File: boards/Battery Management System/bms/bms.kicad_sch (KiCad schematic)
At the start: 25 parts, among them J1 Screw_Terminal_01x05, J2 1986660-2, J3 1986660-2, K1 HE1AN-W-DC6V-Y6, U1 BD48L32G, U2 BD48L32G, U3 BD48L32G, U4 BD48L32G, U5 SN74HC08DR, U6 TL071HIDBVR

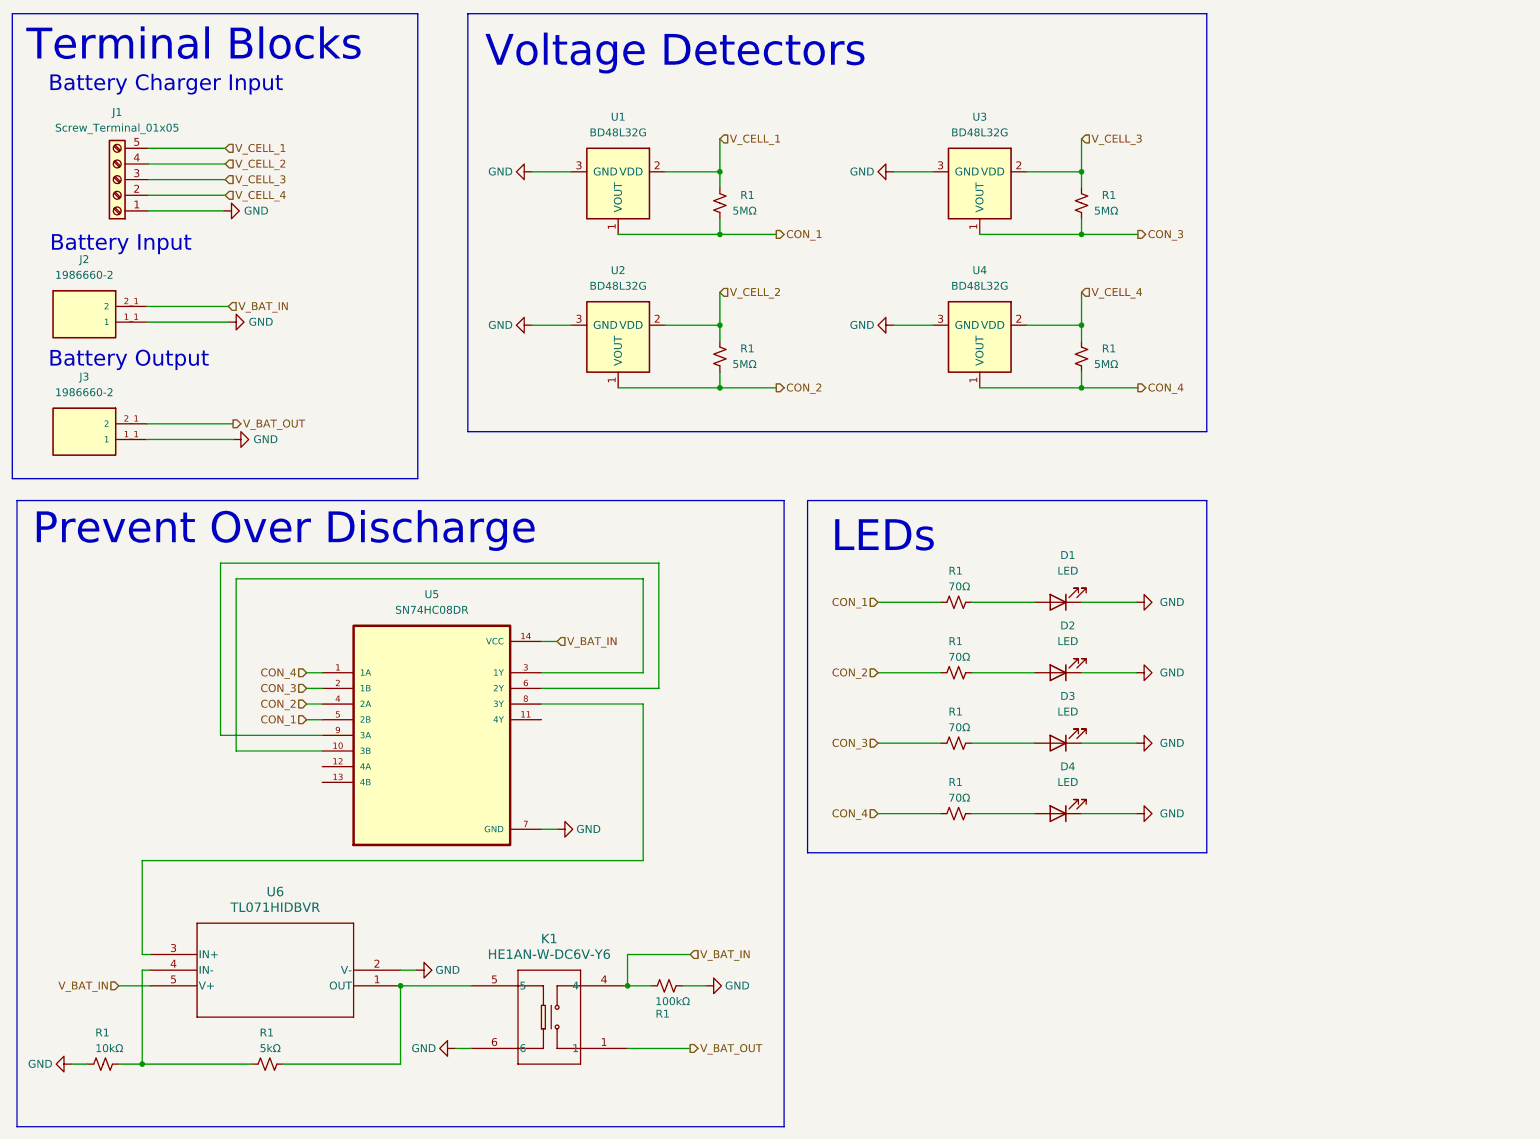
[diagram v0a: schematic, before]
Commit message: Removed Relay
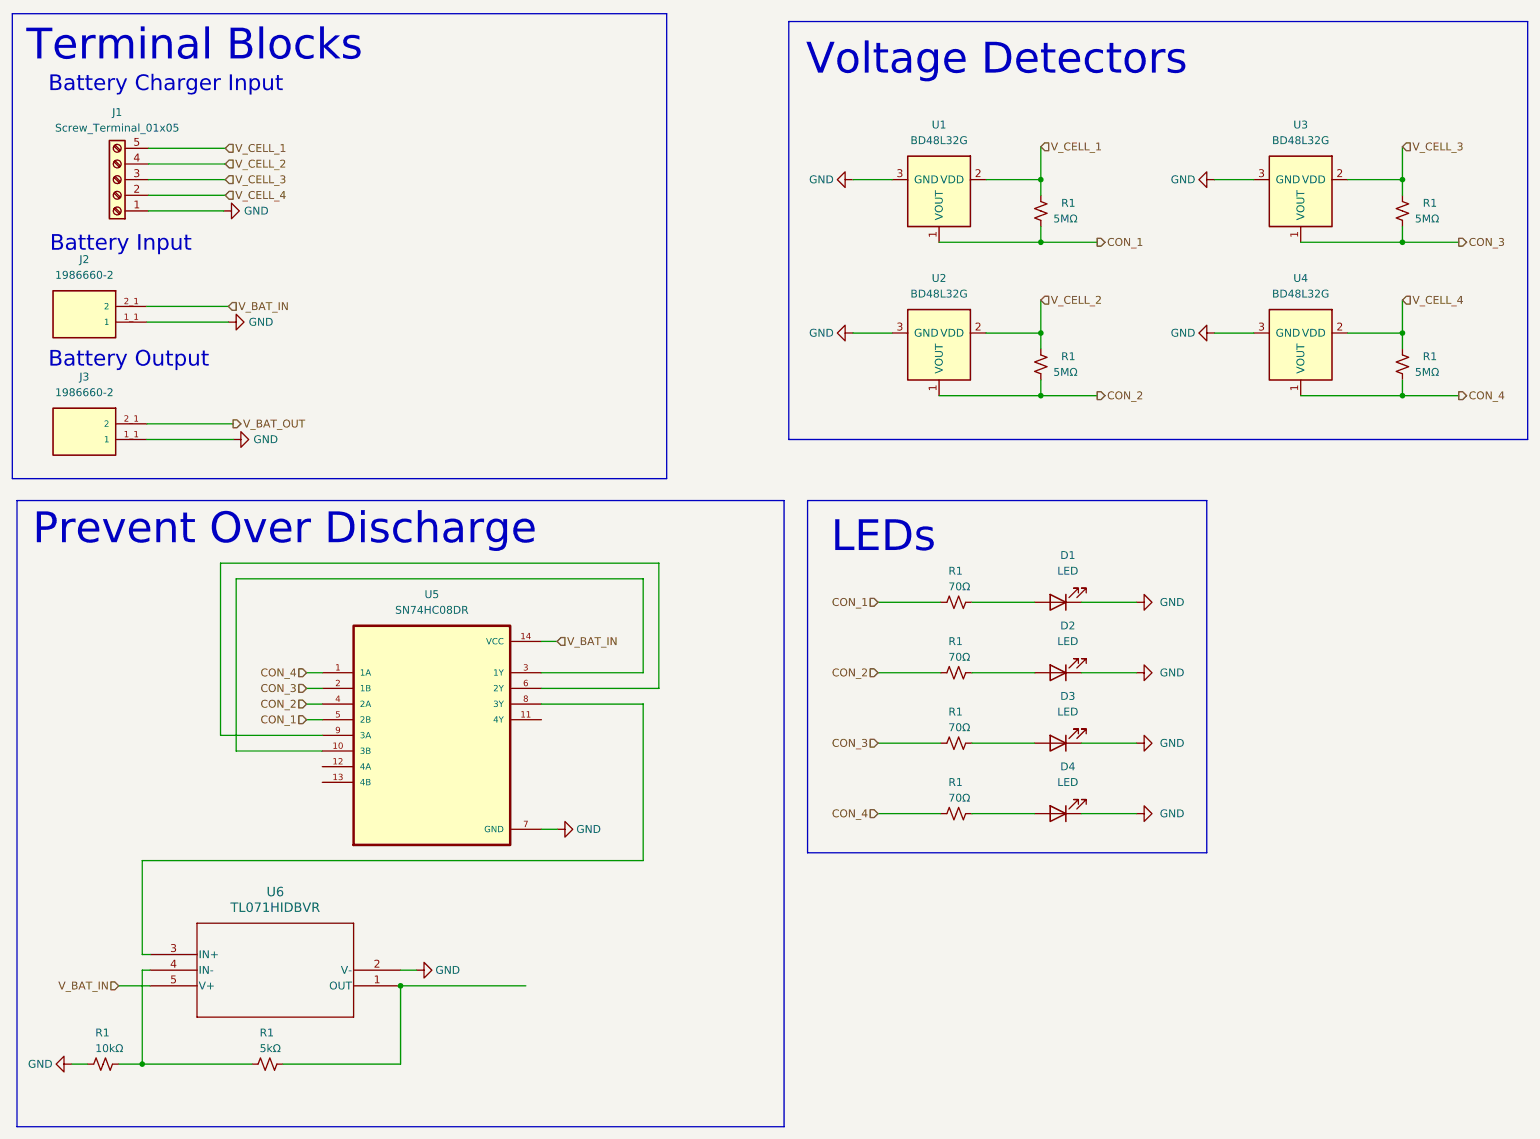
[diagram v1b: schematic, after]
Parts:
- removed K1: HE1AN-W-DC6V-Y6, HE1AN_W_DC6V_Y6:HE1AN-W-DC6V_PAN, symbol 2024-03-08_00-12-08:HE1AN-W-DC6V-Y6
- removed R1: 100kΩ, Resistor_SMD:R_0805_2012Metric, symbol Device:R_Small_US
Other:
- moved on the sheet: R1, U1, U2, U3, U4

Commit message: New Schematic
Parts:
- removed J2, J3: 1986660-2, 1986660_2a:TE_1986660-2, symbol 1986660-2:1986660-2
- removed R1: 10kΩ, Resistor_SMD:R_0805_2012Metric, symbol Device:R_Small_US
- removed R1: 5kΩ, Resistor_SMD:R_0805_2012Metric, symbol Device:R_Small_US
- removed U6: TL071HIDBVR, TL071HIDBVR:SOT23_DBV_5_TEX-L, symbol TL071HIDBVR:TL071HIDBVR
- J1: value Screw_Terminal_01x05 -> Screw_Terminal_01x06; symbol Connector:Screw_Terminal_01x05 -> Connector:Screw_Terminal_01x06
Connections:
- net V_OUT: now reaches U5.8 (3Y)
- net V_OUT: now also J1.6 (Pin_6)
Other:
- note removed: "Battery Input"
- note removed: "Battery Output"

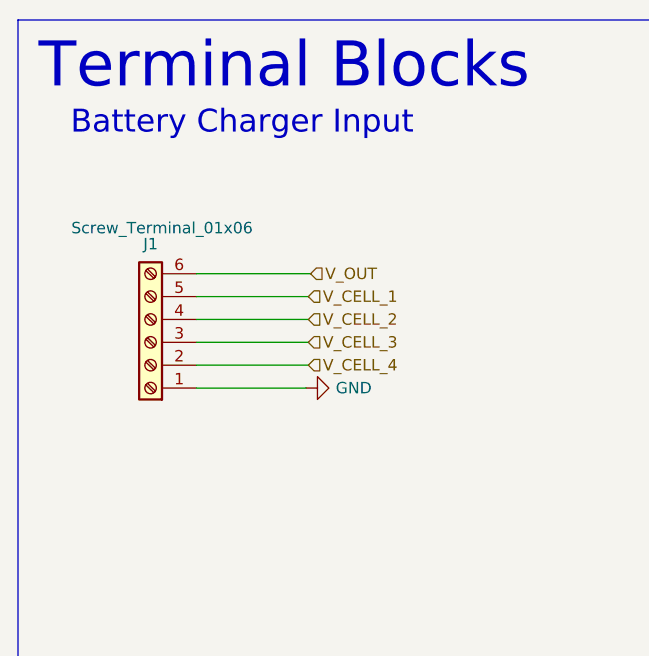
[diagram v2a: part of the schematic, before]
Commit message: Changed JST onnector
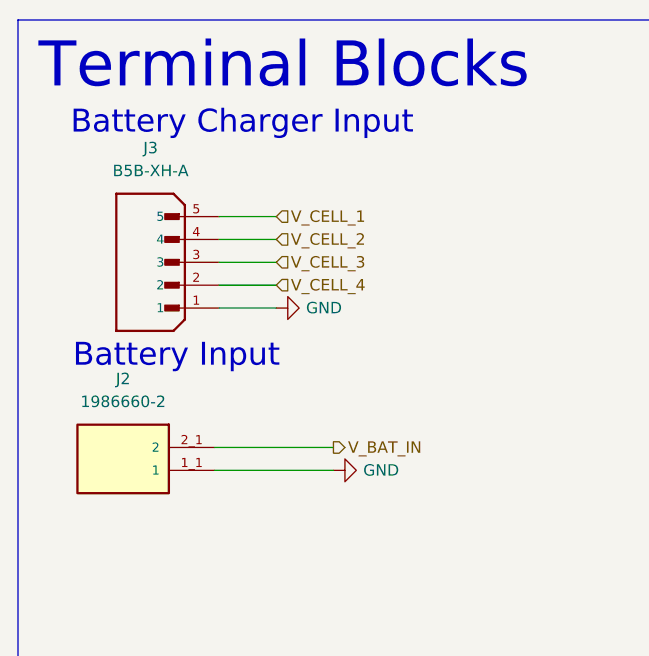
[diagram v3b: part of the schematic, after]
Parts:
- removed J1: Screw_Terminal_01x06, B5B_XH_A:JST_B5B-XH-A, symbol Connector:Screw_Terminal_01x06
- added J2: 1986660-2, 1986660_2a:TE_1986660-2, symbol 1986660-2:1986660-2
- added J3: B5B-XH-A, B5B-XH-A:JST_B5B-XH-A, symbol B5B-XH-A:B5B-XH-A
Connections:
- net GND: now also J2.1_1 (1), J3.1
- net V_BAT_IN: now also J2.2_1 (2)
- net V_CELL_1: now also J3.5
- net V_CELL_2: now also J3.4
- net V_CELL_3: now also J3.3
- net V_CELL_4: now also J3.2
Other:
- note added: "Battery Input"

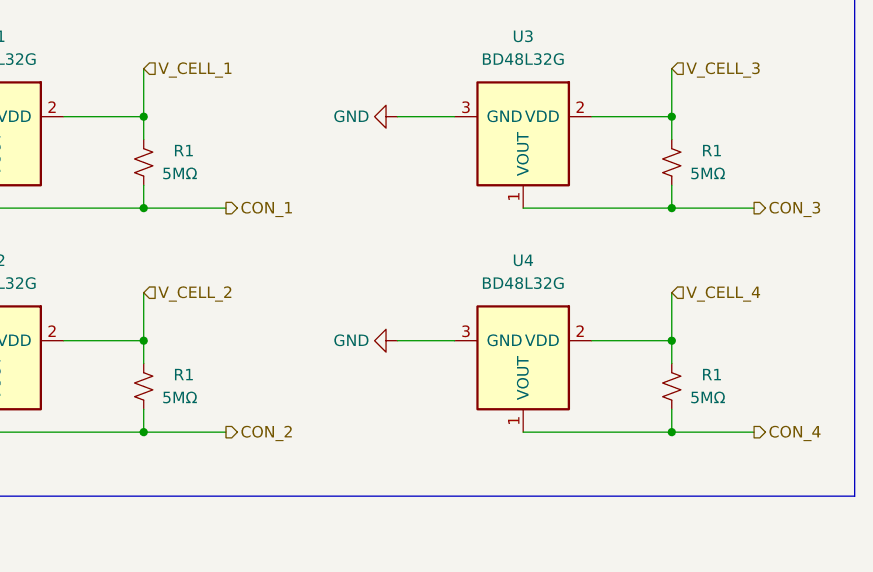
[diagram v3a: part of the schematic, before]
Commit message: Changed Resistors
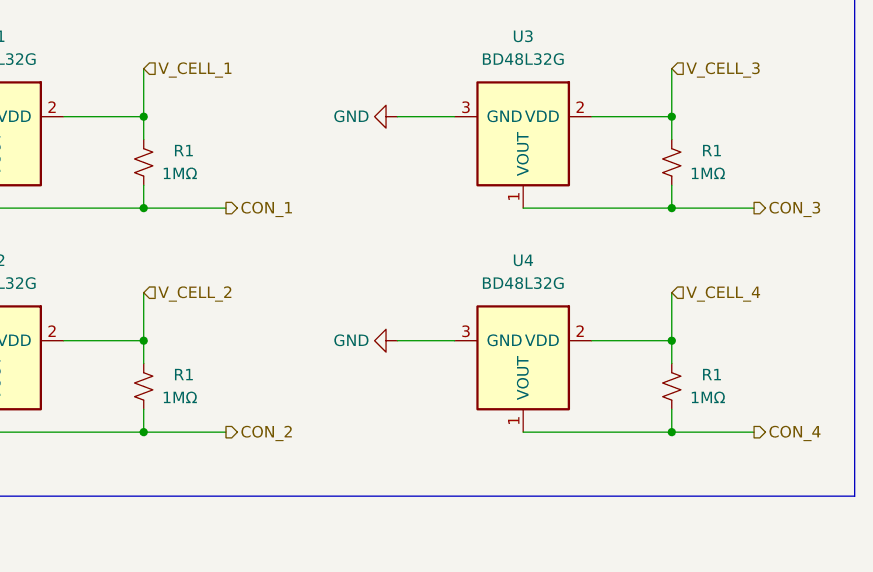
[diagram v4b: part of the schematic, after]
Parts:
- R1: value 5MΩ -> 1MΩ
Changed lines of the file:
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@@
 			)
 		)
-		(property "Value" "5MΩ"
+		(property "Value" "1MΩ"
 			(at 189.738 73.152 0)
 			(effects
@@
 			)
 		)
-		(property "Value" "5MΩ"
+		(property "Value" "1MΩ"
 			(at 248.412 73.152 0)
 			(effects
@@
 			)
 		)
-		(property "Value" "5MΩ"
+		(property "Value" "1MΩ"
 			(at 248.412 48.26 0)
 			(effects
@@
 			)
 		)
-		(property "Value" "5MΩ"
+		(property "Value" "1MΩ"
 			(at 189.738 48.26 0)
 			(effects

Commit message: BMS Changes
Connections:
- net GND: no longer D1.1 (K), D2.1 (K), D3.1 (K), J2.1_1 (1), U1.3 (GND), U2.3 (GND), U3.3 (GND), U5.7 (GND)
- net V_CELL_1: now also U5.14 (VCC)
- net V_CELL_2: now also D1.1 (K), J2.1_1 (1), U1.3 (GND), U5.7 (GND)
- net V_CELL_3: now also D2.1 (K), U2.3 (GND)
- net V_CELL_4: now also D3.1 (K), U3.3 (GND)
- net V_OUT: now also J2.2_1 (2)
- removed net V_BAT_IN: J2.2_1 (2), U5.14 (VCC)
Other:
- note added: "Relay Input"
- note removed: "Battery Input"
- moved on the sheet: J2, R1, U2

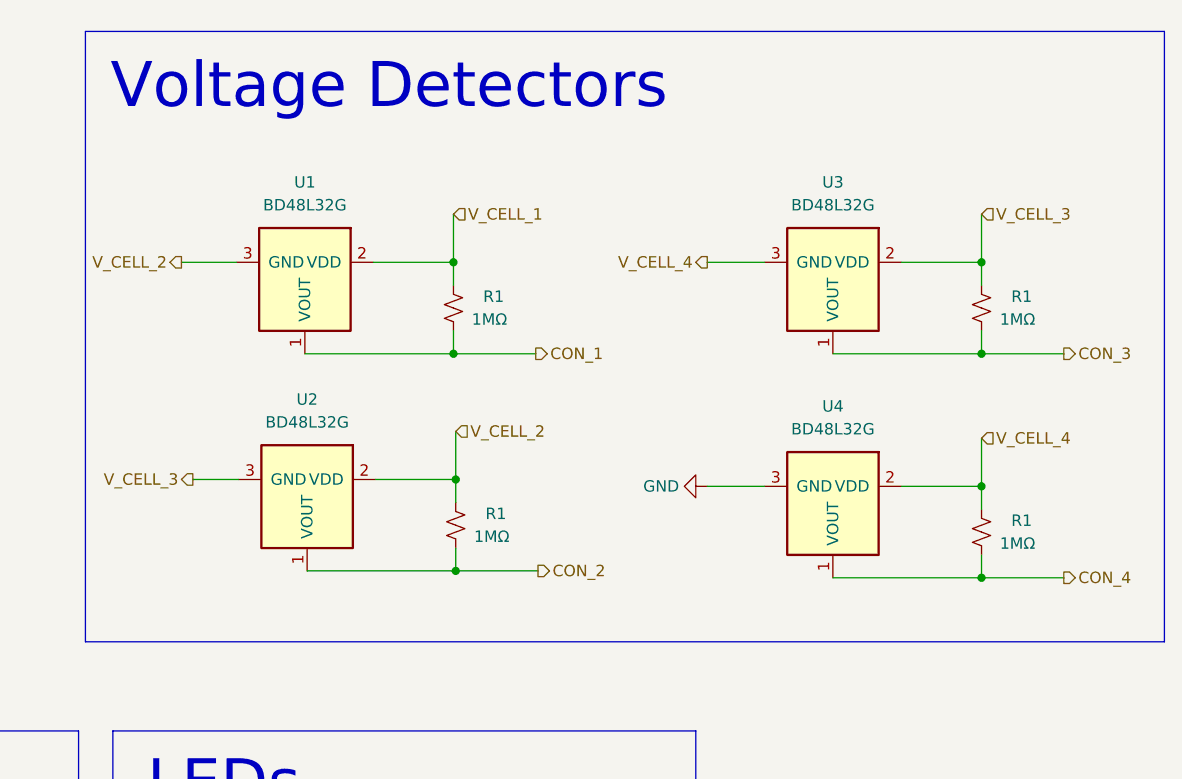
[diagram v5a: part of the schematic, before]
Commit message: BMS updated circuit
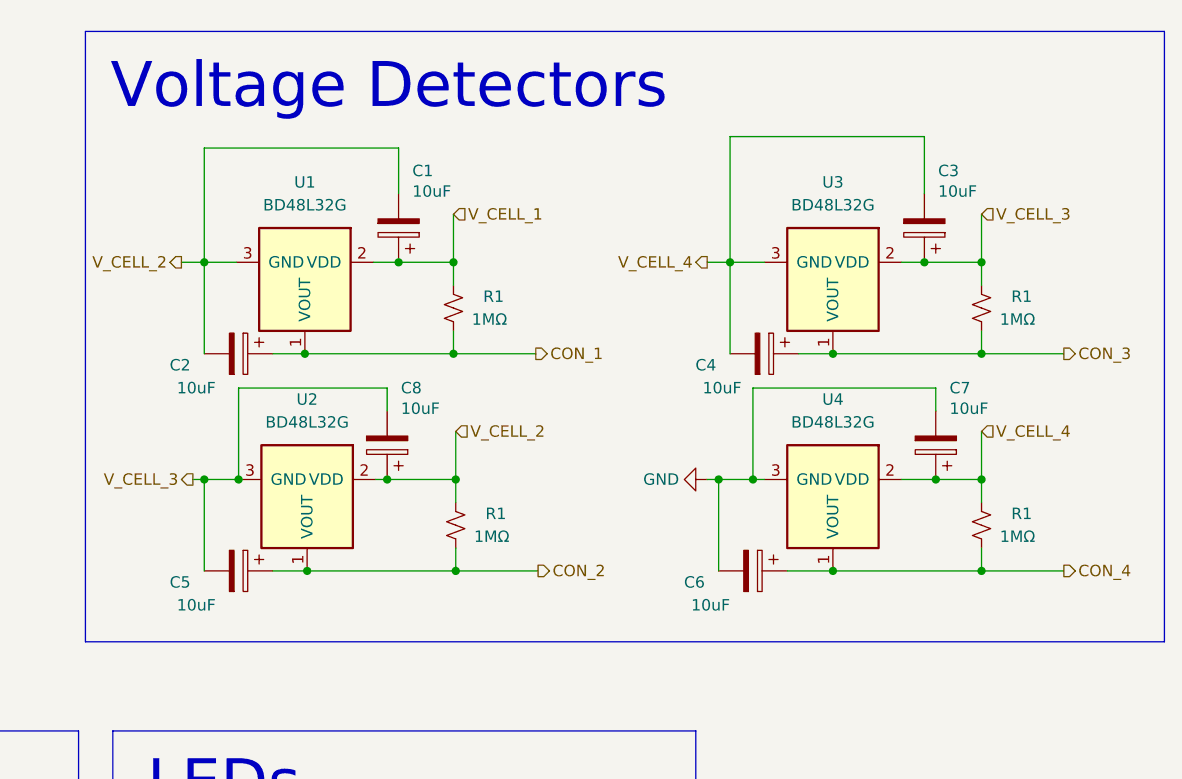
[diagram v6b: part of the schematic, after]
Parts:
- added C1, C2, C3, C4, C5, C6, C7, C8: 10uF, Capacitor_SMD:C_0805_2012Metric, symbol Device:C_Polarized
- J2: footprint 1986660_2a:TE_1986660-2 -> 1986660_2:TE_1986660-2
- J3: footprint B5B-XH-A:JST_B5B-XH-A -> Connector_JST:JST_XH_B5B-XH-A_1x05_P2.50mm_Vertical
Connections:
- net CON_1: now also C2.1
- net CON_2: now also C5.1
- net CON_3: now also C4.1
- net CON_4: now also C6.1
- net GND: now also C6.2, C7.2
- net V_CELL_1: now also C1.1
- net V_CELL_2: now also C1.2, C2.2, C8.1
- net V_CELL_3: now also C3.1, C5.2, C8.2
- net V_CELL_4: now also C3.2, C4.2, C7.1
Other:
- moved on the sheet: R1, U4
